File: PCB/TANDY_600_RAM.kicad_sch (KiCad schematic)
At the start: 5 parts, among them J1 DIN 41612 2x22 male right-ang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, U1 628128_SOP, U2 74HC08

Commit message: gnd on tiny, new dual sch, bus connector symbol & footprint
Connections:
- net A0: now also J1.b12; no longer J1.12B
- net A1: now also J1.a12; no longer J1.12A
- net A10: now also J1.b6; no longer J1.6B
- net A11: now also J1.a6; no longer J1.6A
- net A12: now also J1.a5; no longer J1.5A
- net A13: now also J1.b4; no longer J1.4B
- net A14: now also J1.a4; no longer J1.4A
- net A2: now also J1.b11; no longer J1.11B
- net A3: now also J1.a11; no longer J1.11A
- net A4: now also J1.a10; no longer J1.10A
- net A5: now also J1.b9; no longer J1.9B
- net A6: now also J1.a9; no longer J1.9A
- net A7: now also J1.b8; no longer J1.8B
- net A8: now also J1.b7; no longer J1.7B
- net A9: now also J1.a7; no longer J1.7A
- net CS2: now also J1.b21; no longer J1.21B
- net D0: now also J1.b17; no longer J1.17B
- net D1: now also J1.a17; no longer J1.17A
- net D2: now also J1.b16; no longer J1.16B
- net D3: now also J1.a16; no longer J1.16A
- net D4: now also J1.a15; no longer J1.15A
- net D5: now also J1.b14; no longer J1.14B
- net D6: now also J1.a14; no longer J1.14A
- net D7: now also J1.b13; no longer J1.13B
- net GND: now also J1.M1 (mount), J1.M2 (mount), J1.a13, J1.a18, J1.a19, J1.a22, J1.a3, J1.a8, J1.b10, J1.b22, J1.b5; no longer J1.10B, J1.13A, J1.18A, J1.19A, J1.22A, J1.22B, J1.3A, J1.5B, J1.8A, J1.S1 (mount), J1.S2 (mount)
- net VCC: now also J1.a2, J1.b2; no longer J1.2A, J1.2B
- net VMEM: now also J1.a1, J1.b1; no longer J1.1A, J1.1B
- net ~{CS1_A}: now also J1.b3; no longer J1.3B
- net ~{CS1_B}: now also J1.b20; no longer J1.20B
- net ~{CS1_C}: now also J1.a20; no longer J1.20A
- net ~{OE}: now also J1.b18; no longer J1.18B
- net ~{WE}: now also J1.b19; no longer J1.19B
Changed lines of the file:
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@@
   (title_block
     (title "96K RAM for TANDY 600")
-    (date "2022-09-27")
-    (rev "010")
+    (date "2022-10-04")
+    (rev "SMT_011")
     (company "Brian K. White - b.kenyon.w@gmail.com")
     (comment 1 "LICENSE: CC-BY-SA 4.0")
@@
     (pin "2")
   )
-  (symbol (lib_id "000_LOCAL:DIN 41612 2x22 male right-angle") (at 69.85 83.82 0) (unit 1)
+  (symbol (lib_id "000_LOCAL:DIN 41612 2x22 male right-angle") (at 71.12 85.09 0) (unit 1)
     (in_bom yes) (on_board yes)
-    (property "Reference" "J1" (id 0) (at 71.628 46.99 0))
-    (property "Value" "DIN 41612 2x22 male right-angle" (id 1) (at 71.882 49.657 0))
-    (property "Footprint" "000_LOCAL:DIN 41612 2x22 male right-angle" (id 2) (at 69.85 83.82 0)
+    (property "Reference" "J1" (id 0) (at 72.898 48.26 0))
+    (property "Value" "DIN 41612 2x22 male right-angle" (id 1) (at 73.152 50.927 0))
+    (property "Footprint" "000_LOCAL:DIN 41612 2x22 male right-angle" (id 2) (at 71.12 85.09 0)
       (effects (font (size 1.27 1.27)) hide)
     )
-    (property "Datasheet" "~" (id 3) (at 69.85 83.82 0)
+    (property "Datasheet" "~" (id 3) (at 71.12 85.09 0)
       (effects (font (size 1.27 1.27)) hide)
     )
-    (pin "10A")
-    (pin "10B")
-    (pin "11A")
-    (pin "11B")
-    (pin "12A")
-    (pin "12B")
-    (pin "13A")
-    (pin "13B")
-    (pin "14A")
-    (pin "14B")
-    (pin "15A")
-    (pin "15B")
-    (pin "16A")
-    (pin "16B")
-    (pin "17A")
-    (pin "17B")
-    (pin "18A")
-    (pin "18B")
-    (pin "19A")
-    (pin "19B")
-    (pin "1A")
-    (pin "1B")
-    (pin "20A")
-    (pin "20B")
-    (pin "21A")
-    (pin "21B")
-    (pin "22A")
-    (pin "22B")
-    (pin "2A")
-    (pin "2B")
-    (pin "3A")
-    (pin "3B")
-    (pin "4A")
-    (pin "4B")
-    (pin "5A")
-    (pin "5B")
-    (pin "6A")
-    (pin "6B")
-    (pin "7A")
-    (pin "7B")
-    (pin "8A")
-    (pin "8B")
-    (pin "9A")
-    (pin "9B")
-    (pin "S1")
-    (pin "S2")
+    (pin "M1")
+    (pin "M2")
+    (pin "a1")
+    (pin "a10")
+    (pin "a11")
+    (pin "a12")
+    (pin "a13")
+    (pin "a14")
+    (pin "a15")
+    (pin "a16")
+    (pin "a17")
+    (pin "a18")
+    (pin "a19")
+    (pin "a2")
+    (pin "a20")
+    (pin "a21")
+    (pin "a22")
+    (pin "a3")
+    (pin "a4")
+    (pin "a5")
+    (pin "a6")
+    (pin "a7")
+    (pin "a8")
+    (pin "a9")
+    (pin "b1")
+    (pin "b10")
+    (pin "b11")
+    (pin "b12")
+    (pin "b13")
+    (pin "b14")
+    (pin "b15")
+    (pin "b16")
+    (pin "b17")
+    (pin "b18")
+    (pin "b19")
+    (pin "b2")
+    (pin "b20")
+    (pin "b21")
+    (pin "b22")
+    (pin "b3")
+    (pin "b4")
+    (pin "b5")
+    (pin "b6")
+    (pin "b7")
+    (pin "b8")
+    (pin "b9")
   )
   (symbol (lib_id "000_LOCAL:VMEM") (at 64.77 58.42 90) (unit 1)

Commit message: add full-size dual
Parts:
- J1: symbol 000_LOCAL:DIN 41612 2x22 male right-angle -> 000_LOCAL:DIN_41612_02x22
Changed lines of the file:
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@@
     (pin "2")
   )
-  (symbol (lib_id "000_LOCAL:DIN 41612 2x22 male right-angle") (at 71.12 85.09 0) (unit 1)
+  (symbol (lib_id "000_LOCAL:DIN_41612_02x22") (at 71.12 85.09 0) (unit 1)
     (in_bom yes) (on_board yes)
     (property "Reference" "J1" (id 0) (at 72.898 48.26 0))
     (property "Value" "DIN 41612 2x22 male right-angle" (id 1) (at 73.152 50.927 0))
-    (property "Footprint" "000_LOCAL:DIN 41612 2x22 male right-angle" (id 2) (at 71.12 85.09 0)
+    (property "Footprint" "000_LOCAL:DIN 41612 2x22 male right-angle" (id 2) (at 69.85 83.82 0)
       (effects (font (size 1.27 1.27)) hide)
     )
-    (property "Datasheet" "~" (id 3) (at 71.12 85.09 0)
+    (property "Datasheet" "~" (id 3) (at 69.85 83.82 0)
       (effects (font (size 1.27 1.27)) hide)
     )

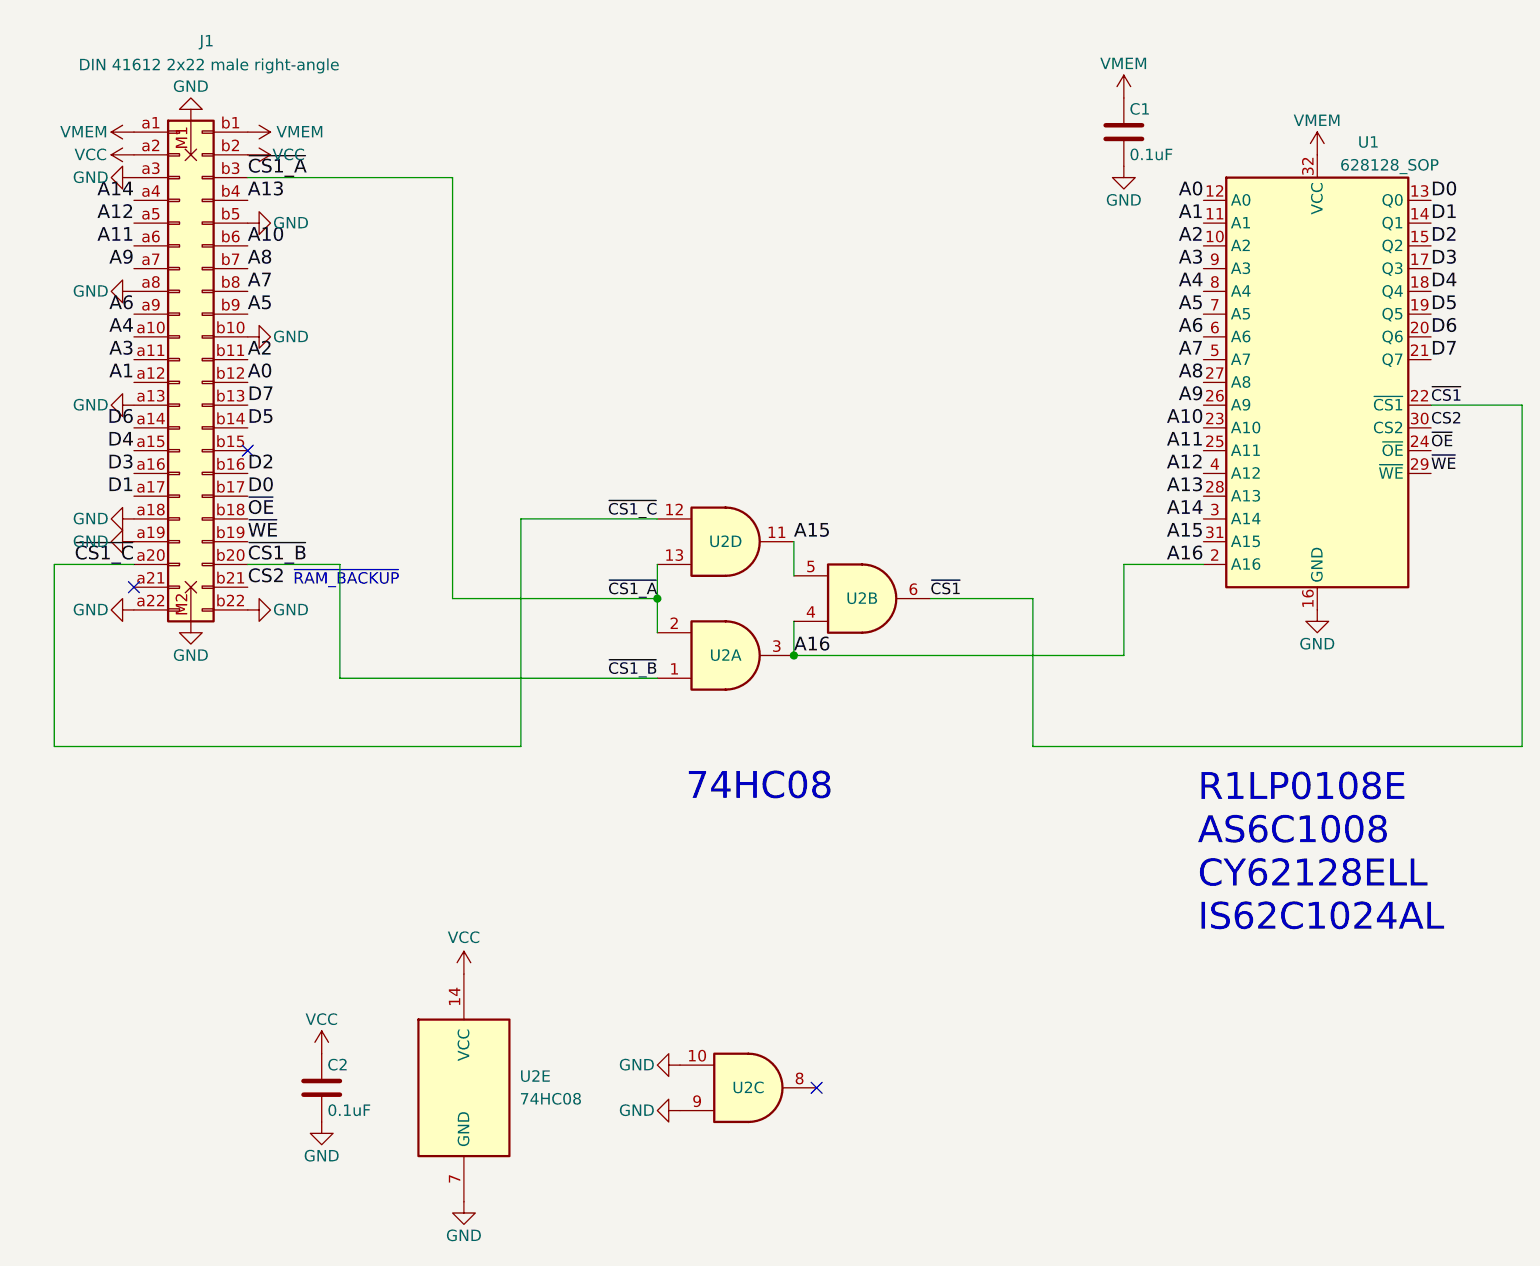
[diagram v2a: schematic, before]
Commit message: footprints, ground paths
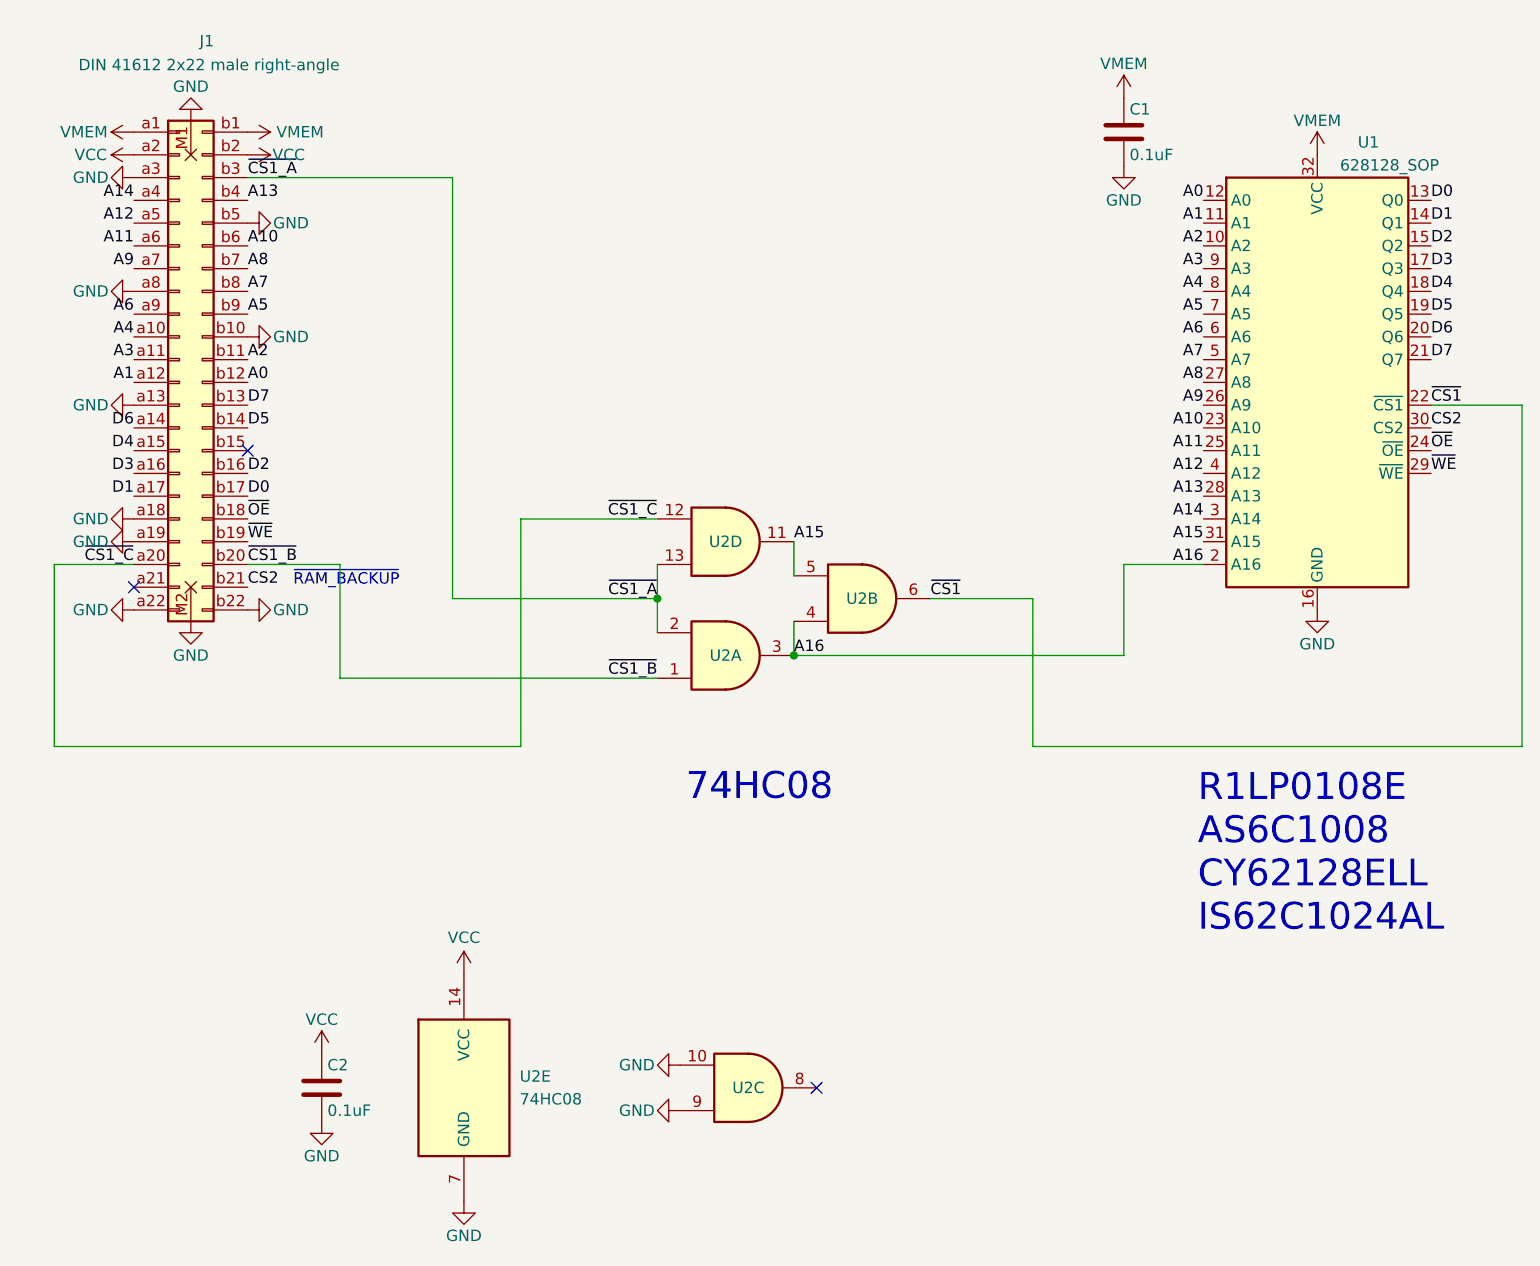
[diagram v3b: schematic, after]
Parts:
- J1: footprint 000_LOCAL:DIN 41612 2x22 male right-angle -> 000_LOCAL:DIN-41612_02x22_male_horizontal

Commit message: dual_008
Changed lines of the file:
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@@
   (junction (at 123.19 110.49) (diameter 0) (color 0 0 0 0)
+  )
+  (junction (at 138.43 104.14) (diameter 0) (color 0 0 0 0)
   )
   (no_connect (at 140.97 165.1))
@@
     (stroke (width 0) (type default) (color 0 0 0 0))
   )
+  (wire (pts (xy 138.43 104.14) (xy 184.15 104.14))
+    (stroke (width 0) (type default) (color 0 0 0 0))
+  )

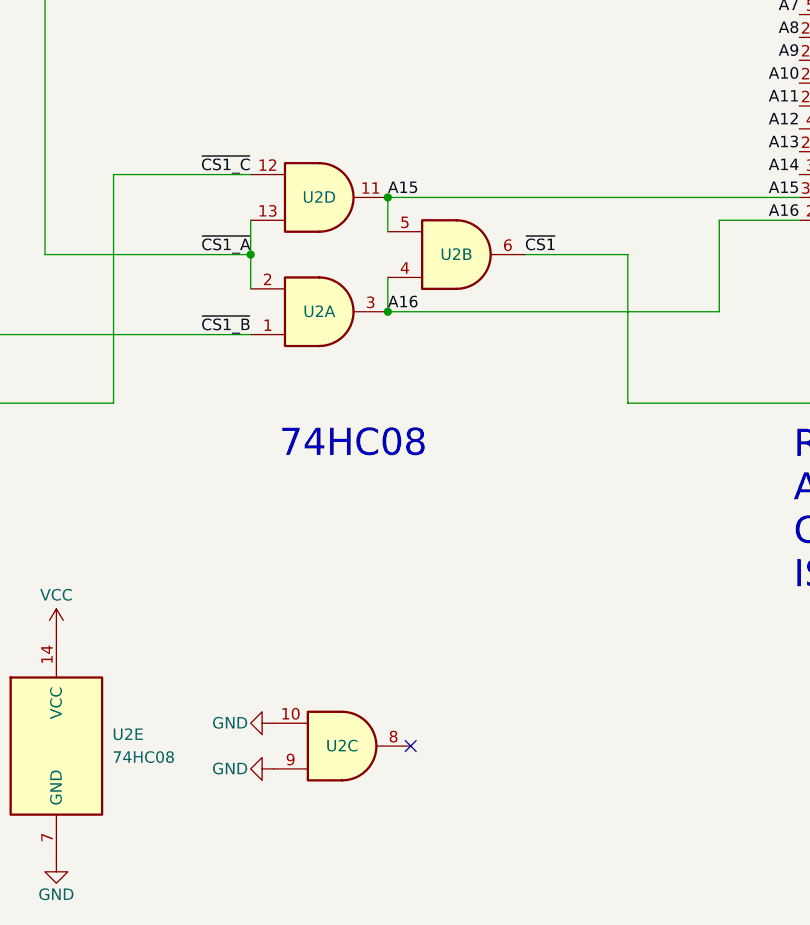
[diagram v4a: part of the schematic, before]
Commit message: dual version add /CE pullup for battery life
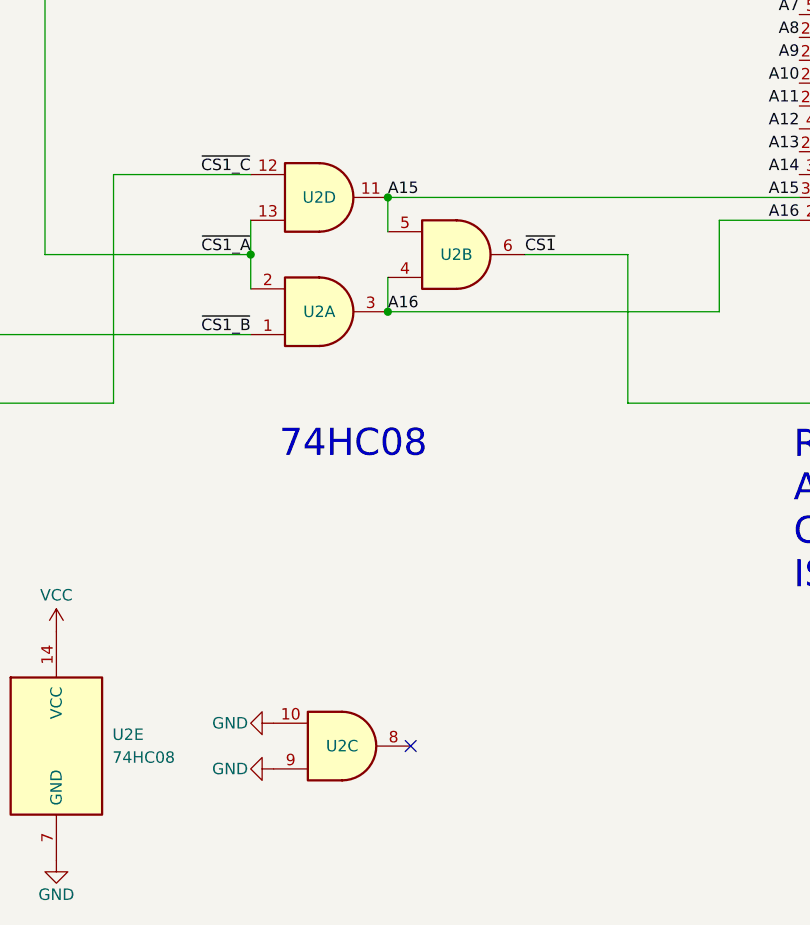
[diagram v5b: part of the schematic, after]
